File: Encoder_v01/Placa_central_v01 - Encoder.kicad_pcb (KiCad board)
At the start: 2 copper layers, 64 parts, among them J1 Conn_01x01_Female, J2 Conn_01x01_Female, J3 Conn_01x01_Female, J4 Conn_01x01_Female, J5 Conn_01x01_Female, J6 Conn_01x01_Female, U1 TCRT5000Esq, U2 LM741Esq, U3 TCRT5000Dir, U4 LM741

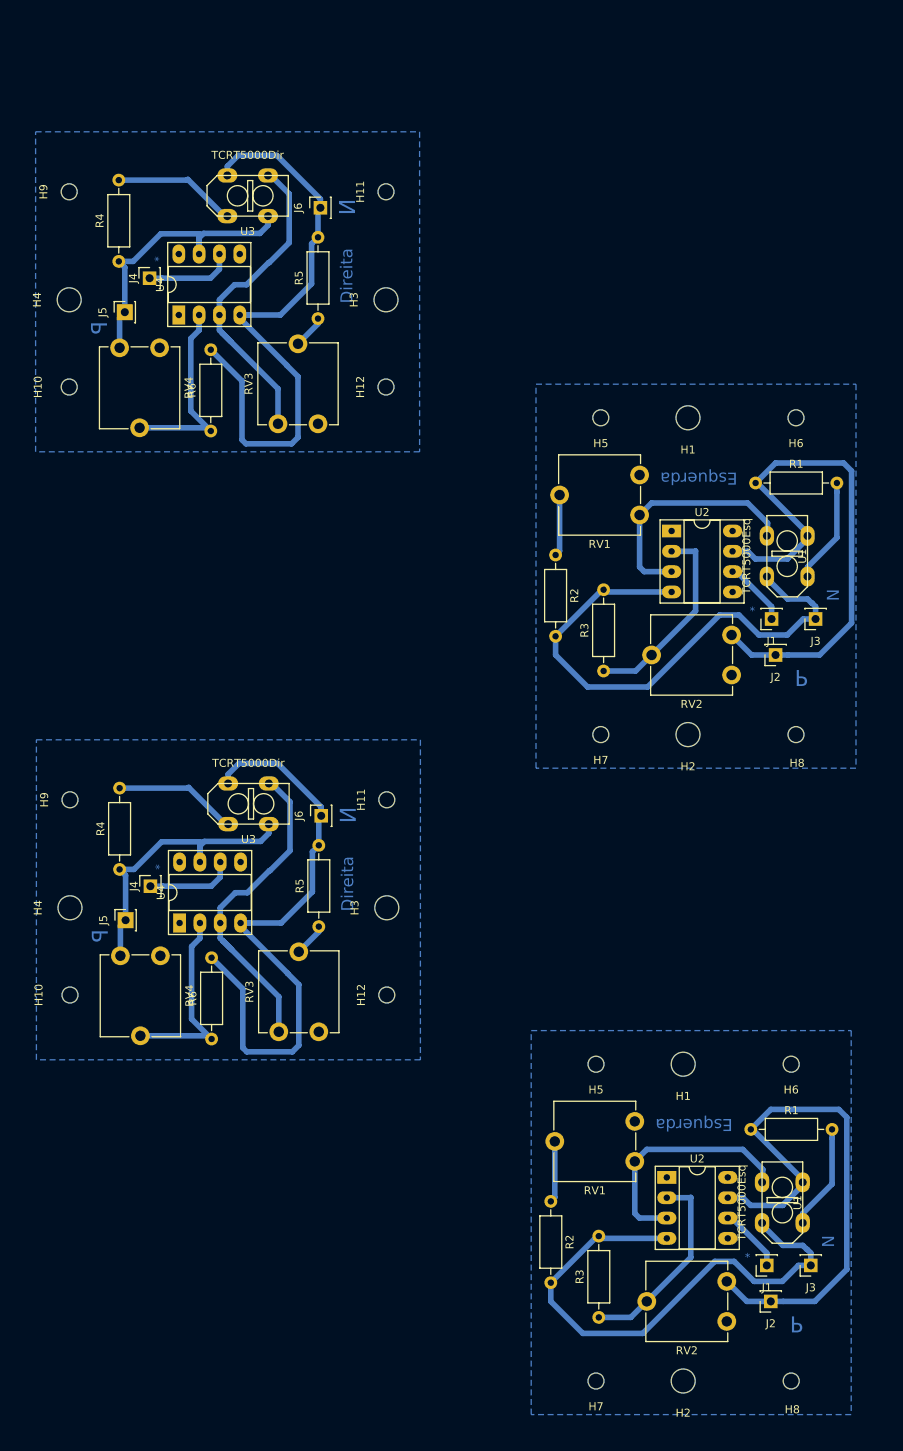
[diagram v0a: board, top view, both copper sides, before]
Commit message: Preparação da placa encoder para impressão
E mexido na placa central: adicionado gnd na placa de cima e keep out area
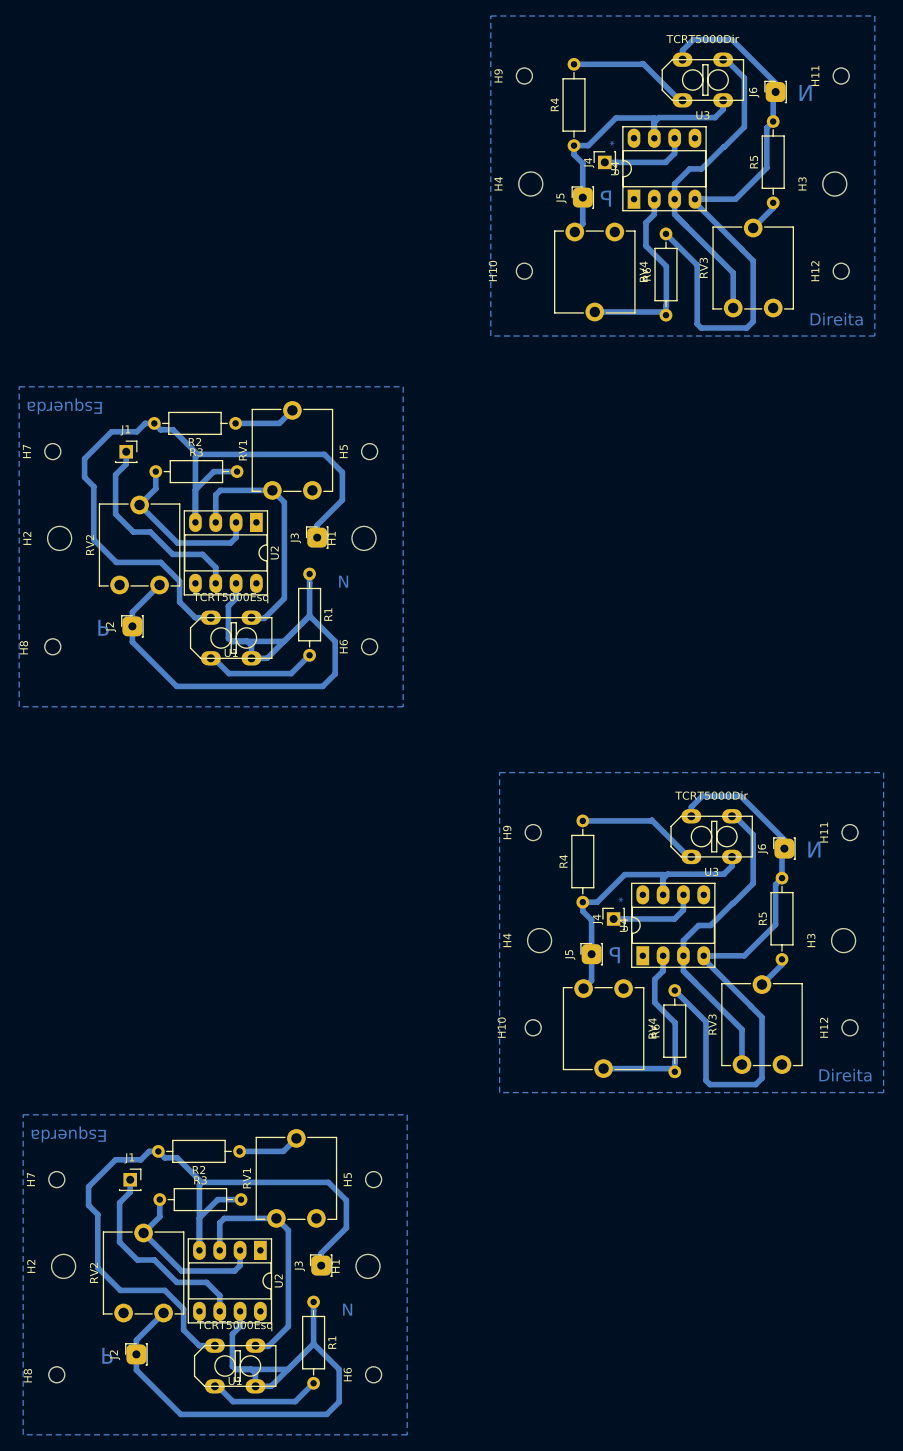
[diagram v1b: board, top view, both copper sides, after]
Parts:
- removed the H2 at (98.5, 183.7)
- removed the H2 at (99.0, 102.8)
- removed the H6 at (112.0, 144.1)
- removed the H6 at (112.5, 63.2)
- removed the H8 at (112.0, 183.7)
- removed the H8 at (112.5, 102.8)
- removed the J1 at (108.9, 169.2)
- removed the J1 at (109.5, 88.4)
- removed the J2 at (109.4, 173.7)
- removed the J2 at (110.0, 92.9)
- added H2: Furo2Esq, MountingHole:MountingHole_3mm, F.Cu at (21.0, 169.3)
- added H2: Furo2Esq, MountingHole:MountingHole_3mm, F.Cu at (20.5, 78.3)
- added H6: Furo4Esq, MountingHole:MountingHole_2mm, F.Cu at (59.8, 182.9)
- added H6: Furo4Esq, MountingHole:MountingHole_2mm, F.Cu at (59.2, 91.9)
- added H8: Furo6Esq, MountingHole:MountingHole_2mm, F.Cu at (20.1, 182.9)
- added H8: Furo6Esq, MountingHole:MountingHole_2mm, F.Cu at (19.6, 91.9)
- added J1: Conn_01x01_Female, Connector_PinSocket_2.54mm:PinSocket_1x01_P2.54mm_Vertical, F.Cu at (29.3, 158.5)
- added J1: Conn_01x01_Female, Connector_PinSocket_2.54mm:PinSocket_1x01_P2.54mm_Vertical, F.Cu at (28.8, 67.5)
- added J2: Conn_01x01_Female, Connector_PinSocket_2.54mm:PinSocket_1x01_P2.54mm_Vertical, F.Cu at (30.1, 180.3)
- added J2: Conn_01x01_Female, Connector_PinSocket_2.54mm:PinSocket_1x01_P2.54mm_Vertical, F.Cu at (29.6, 89.3)
- moved H7 77.1 mm to (19.6, 67.5), turned to 90 degrees
- moved H7 71.9 mm to (20.1, 158.5), turned to 90 degrees
- moved RV2 71.8 mm to (33.0, 84.2), turned to 90 degrees
- moved U1 71.4 mm to (42.5, 181.8), turned to 180 degrees
- moved RV2 70.5 mm to (33.5, 175.2), turned to 90 degrees
- moved U1 70.2 mm to (42.0, 90.8), turned to 180 degrees
- moved J3 63.1 mm to (52.7, 78.2), turned to 90 degrees
- moved R3 61.3 mm to (32.5, 70.0), turned to 0 degrees
- moved J3 61.2 mm to (53.2, 169.2), turned to 90 degrees
- moved H4 59.5 mm to (79.4, 34.0)
- moved J5 59.0 mm to (85.9, 35.7)
- moved H4 58.8 mm to (80.5, 128.6)
- moved R1 58.8 mm to (52.2, 173.8), turned to 270 degrees
- moved H11 58.7 mm to (118.2, 20.5)
- moved H12 58.7 mm to (118.2, 44.9)
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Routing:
- net GNDEsq: track 137.6 -> 191.3 mm
- net SinalEncoderEsq: track 16.5 -> 51.2 mm
- net VccEsq: track 141.8 -> 166.8 mm
- net Net-(R3-Pad1): track 50.2 -> 42.4 mm
- net Net-(R1-Pad2): track 26.4 -> 28.2 mm
- net VccDir: track 74.8 -> 75.4 mm
- added copper zone on B.Cu, net GNDEsq
- removed copper zone on B.Cu, net (none)

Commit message: Correção nas pcbs
Nome da placa de encoder desinvertido
Trilhas laterais de GND da placa central mais espaçadas nos cantos
Nome da equipe colocado na placa central
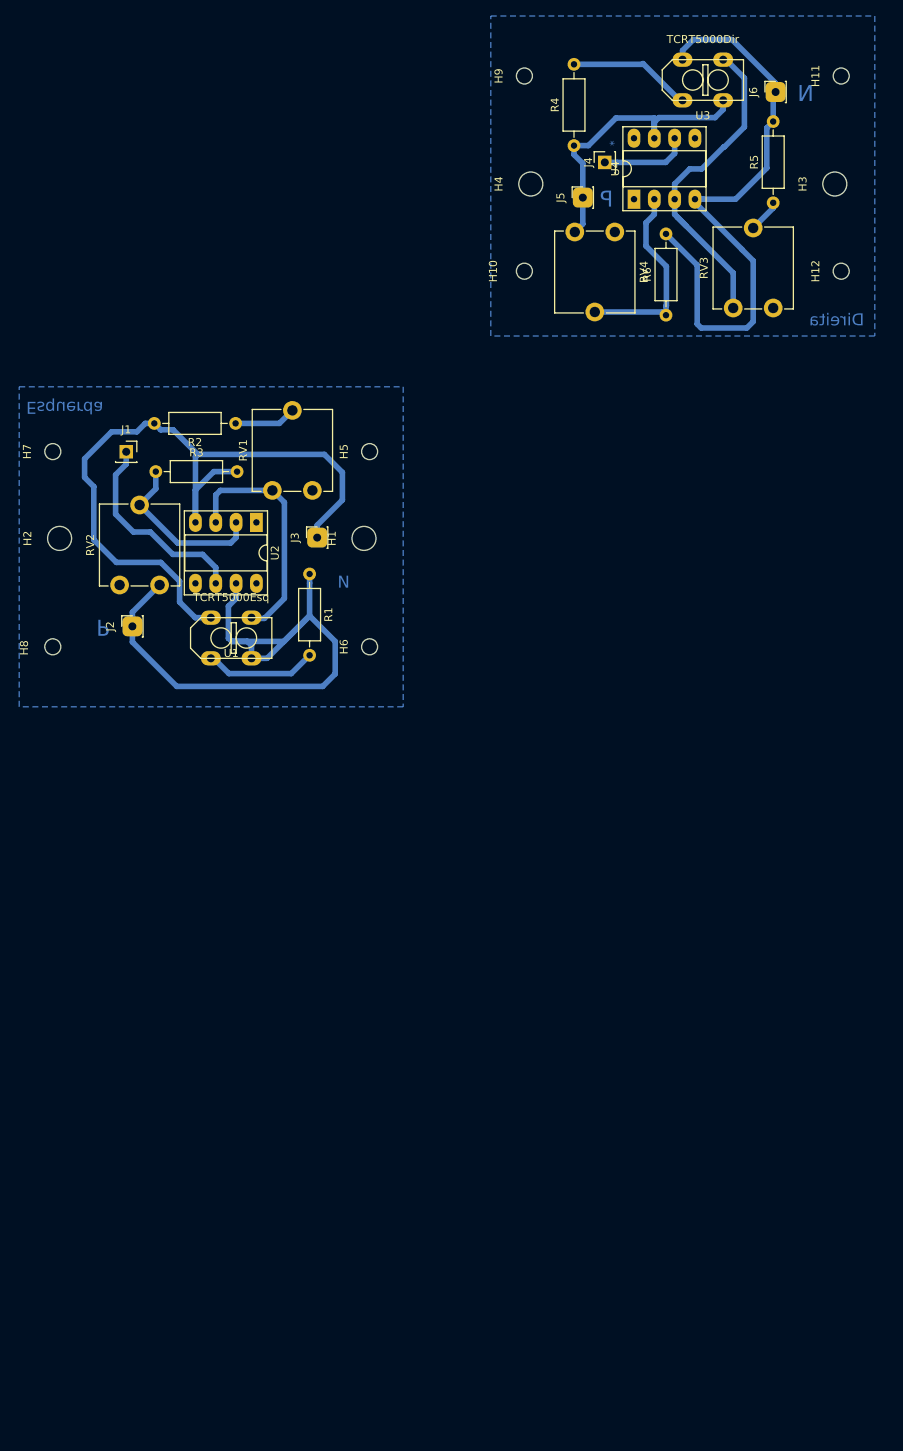
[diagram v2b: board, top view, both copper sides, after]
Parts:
- removed the H1 at (59.0, 169.3)
- removed the H10 at (79.7, 139.5)
- removed the H11 at (119.3, 115.1)
- removed the H12 at (119.3, 139.5)
- removed the H2 at (21.0, 169.3)
- removed the H3 at (118.5, 128.6)
- removed the H4 at (80.5, 128.6)
- removed the H5 at (59.8, 158.5)
- removed the H6 at (59.8, 182.9)
- removed the H7 at (20.1, 158.5)
- removed the H8 at (20.1, 182.9)
- removed the H9 at (79.7, 115.1)
- removed the J1 at (29.3, 158.5)
- removed the J2 at (30.1, 180.3)
- removed the J3 at (53.2, 169.2)
- removed the J4 at (89.8, 125.9)
- removed the J5 at (87.0, 130.3)
- removed the J6 at (111.1, 117.1)
- removed the R1 at (52.2, 173.8)
- removed the R2 at (43.0, 154.9)
- removed the R3 at (33.0, 161.0)
- removed the R4 at (85.9, 123.8)
- removed the R5 at (110.8, 130.9)
- removed the R6 at (97.4, 145.0)
- removed the RV1 at (52.6, 163.3)
- removed the RV2 at (33.5, 175.2)
- removed the RV3 at (110.8, 144.1)
- removed the RV4 at (86.0, 134.6)
- removed the U1 at (42.5, 181.8)
- removed the U2 at (45.6, 167.3)
- removed the U3 at (102.0, 115.6)
- removed the U4 at (93.4, 130.5)
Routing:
- net GNDEsq: track 191.3 -> 95.7 mm
- net VccEsq: track 166.8 -> 83.4 mm
- net GNDDir: track 154.1 -> 77.0 mm
- net Net-(RV3-Pad3): track 83.8 -> 41.9 mm
- net VccDir: track 75.4 -> 37.7 mm
- net Net-(RV1-Pad3): track 60.1 -> 30.0 mm
- net SinalEncoderEsq: track 51.2 -> 25.6 mm
- net Net-(R6-Pad1): track 50.1 -> 25.1 mm
- net Net-(R3-Pad1): track 42.4 -> 21.2 mm
- net Net-(R4-Pad2): track 31.0 -> 15.5 mm
- net Net-(R1-Pad2): track 28.2 -> 14.1 mm
- net SinalEncoderDIr: track 22.2 -> 11.1 mm
- net Net-(R2-Pad1): track 15.5 -> 7.77 mm
- net Net-(R5-Pad1): track 8.37 -> 4.19 mm
